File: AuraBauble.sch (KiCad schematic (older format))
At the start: 19 parts

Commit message: Switched Zener Diodes to a PRTR5V0U2X
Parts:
- removed D? (x5): 3.6V, symbol Device:D_Zener
- added D?: PRTR5V0U2X_215, digikey-footprints:TO-253-4, symbol dk_TVS-Diodes:PRTR5V0U2X_215
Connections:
- wire segments 78 -> 68
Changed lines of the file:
@@
 	9500 2100 9750 2100
 Connection ~ 9750 2100
-Wire Wire Line
-	9750 2100 10250 2100
-Wire Wire Line
-	9900 900  10250 900
 Connection ~ 9900 900
 Wire Wire Line
 	9900 900  9900 850
 Wire Wire Line
-	10250 1650 10250 900
-Connection ~ 10250 900
-Wire Wire Line
-	10250 1950 10250 2100
-Wire Wire Line
-	10250 2100 10550 2100
-Wire Wire Line
-	10550 1950 10550 2100
-Connection ~ 10550 2100
-Wire Wire Line
-	10550 2100 10850 2100
-Wire Wire Line
-	10850 1950 10850 2100
-Wire Wire Line
-	10850 1650 10850 1400
-Connection ~ 10850 1400
-Wire Wire Line
-	10850 1400 10850 1250
-$Comp
-L Device:D_Zener D?
-U 1 1 5F610AD1
-P 10850 1800
-F 0 "D?" V 10804 1880 50  0000 L CNN
-F 1 "3.6V" V 10895 1880 50  0000 L CNN
-F 2 "" H 10850 1800 50  0001 C CNN
-F 3 "~" H 10850 1800 50  0001 C CNN
-	1    10850 1800
-	0    1    1    0
-$EndComp
-$Comp
-L Device:D_Zener D?
-U 1 1 5F6110CF
-P 10550 1800
-F 0 "D?" V 10504 1880 50  0000 L CNN
-F 1 "3.6V" V 10595 1880 50  0000 L CNN
-F 2 "" H 10550 1800 50  0001 C CNN
-F 3 "~" H 10550 1800 50  0001 C CNN
-	1    10550 1800
-	0    1    1    0
-$EndComp
-$Comp
-L Device:D_Zener D?
-U 1 1 5F6115F3
-P 10250 1800
-F 0 "D?" V 10204 1880 50  0000 L CNN
-F 1 "3.6V" V 10295 1880 50  0000 L CNN
-F 2 "" H 10250 1800 50  0001 C CNN
-F 3 "~" H 10250 1800 50  0001 C CNN
-	1    10250 1800
-	0    1    1    0
-$EndComp
-Wire Wire Line
-	9500 1400 10850 1400
-Wire Wire Line
-	10250 900  10550 900
-Wire Wire Line
-	10850 1400 10950 1400
-Wire Wire Line
-	9500 1300 10550 1300
-Wire Wire Line
-	10550 1650 10550 1300
-Connection ~ 10550 1300
-Wire Wire Line
-	10550 1300 10950 1300
-Wire Wire Line
-	10550 1300 10550 1250
-Wire Wire Line
-	10550 950  10550 900
-Connection ~ 10550 900
-Wire Wire Line
-	10550 900  10850 900
-Wire Wire Line
-	10850 950  10850 900
-$Comp
-L Device:D_Zener D?
-U 1 1 5F626D93
-P 10850 1100
-F 0 "D?" V 10804 1180 50  0000 L CNN
-F 1 "3.6V" V 10895 1180 50  0000 L CNN
-F 2 "" H 10850 1100 50  0001 C CNN
-F 3 "~" H 10850 1100 50  0001 C CNN
-	1    10850 1100
-	0    1    1    0
-$EndComp
-$Comp
-L Device:D_Zener D?
-U 1 1 5F62603B
-P 10550 1100
-F 0 "D?" V 10504 1180 50  0000 L CNN
-F 1 "3.6V" V 10595 1180 50  0000 L CNN
-F 2 "" H 10550 1100 50  0001 C CNN
-F 3 "~" H 10550 1100 50  0001 C CNN
-	1    10550 1100
-	0    1    1    0
-$EndComp
+	10750 1950 10750 2100
 Wire Wire Line
 	10100 1800 10100 2200
@@
 	9200 1800 9500 1800
 Connection ~ 9500 1800
-Connection ~ 10250 2100
 Wire Notes Line
 	8750 1750 10000 1750
@@
 Text Notes 8850 4350 0    50   ~ 0
 Programmer may\nhave pullup.
+$Comp
+L dk_TVS-Diodes:PRTR5V0U2X_215 D?
+U 1 1 5F64F554
+P 10550 1450
+F 0 "D?" V 10800 1750 60  0000 L CNN
+F 1 "PRTR5V0U2X_215" H 10150 1950 60  0000 L CNN
+F 2 "digikey-footprints:TO-253-4" H 10750 1650 60  0001 L CNN
+F 3 "https://assets.nexperia.com/documents/data-sheet/PRTR5V0U2X.pdf" H 10750 1750 60  0001 L CNN
+F 4 "1727-3884-1-ND" H 10750 1850 60  0001 L CNN "Digi-Key_PN"
+F 5 "PRTR5V0U2X,215" H 10750 1950 60  0001 L CNN "MPN"
+F 6 "Circuit Protection" H 10750 2050 60  0001 L CNN "Category"
+F 7 "TVS - Diodes" H 10750 2150 60  0001 L CNN "Family"
+F 8 "https://assets.nexperia.com/documents/data-sheet/PRTR5V0U2X.pdf" H 10750 2250 60  0001 L CNN "DK_Datasheet_Link"
+F 9 "/product-detail/en/nexperia-usa-inc/PRTR5V0U2X,215/1727-3884-1-ND/1589981" H 10750 2350 60  0001 L CNN "DK_Detail_Page"
+F 10 "TVS DIODE 5.5V SOT143B" H 10750 2450 60  0001 L CNN "Description"
+F 11 "Nexperia USA Inc." H 10750 2550 60  0001 L CNN "Manufacturer"
+F 12 "Active" H 10750 2650 60  0001 L CNN "Status"
+	1    10550 1450
+	0    1    -1   0
+$EndComp
+Wire Wire Line
+	9500 1400 10250 1400
+Wire Wire Line
+	9500 1300 10250 1300
+Wire Wire Line
+	9900 900  10750 900
+Wire Wire Line
+	10750 900  10750 950
+Wire Wire Line
+	9750 2100 10750 2100
+Wire Wire Line
+	10250 1300 10250 950
+Wire Wire Line
+	10250 950  10350 950
+Wire Wire Line
+	10250 1400 10250 1950
+Wire Wire Line
+	10250 1950 10350 1950
 $EndSCHEMATC

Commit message: Power work.
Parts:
- added D1: BAT54XV2T1G, symbol Device:D_Schottky
- added Q1: Q_NMOS_DGS, symbol Device:Q_NMOS_DGS
- added R1: 1MΩ, symbol Device:R_US
- added R2: 330Ω, symbol Device:R_US
- added U1: LP5912-3.3DRV, Package_SON:WSON-6-1EP_2x2mm_P0.65mm_EP1x1.6mm_ThermalVias, symbol Regulator_Linear:LP5912-3.3DRV
- gave numbers to parts that had none: 15
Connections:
- net GND: now also D2.1 (GND), Q1.3 (S), R1.1, U1.5 (GND), U1.7 (EP)
- net VBUS: now also R2.2, U1.6 (IN)
- net VCC: now also D1.1 (K), U1.1 (OUT); no longer J2.5 (Vref)
- net MOSI: now reaches U2.A3 (PA04)
- net SCK: now reaches U2.A4 (PA06)
- net MISO: now reaches U2.B2 (PA05)
- net ~SS~: now reaches U2.B3 (PA07)
- net USB_POWER: now reaches U2.D3 (PA23)
- net USB_POWER: now also U1.3 (PG)
- net at C5.2, J1.5 (Shield), R4.1: no longer D2.1 (GND)
- new net: Q1.1 (D), R2.1, U1.4 (EN)
- new net +3V3: D1.2 (A), J2.5 (Vref), Q1.2 (G), R1.2
- no-connect marks 1 -> 11
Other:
- note added: "NYI"
- note added: "SPI For ARGB LEDs [26]"
- moved on the sheet: R3

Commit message: Schematic nearly r0.
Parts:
- removed Q1: Q_NMOS_DGS, symbol Device:Q_NMOS_DGS
- added BP1: Close If Option B Selected, symbol Jumper:SolderJumper_2_Open
- added C1, C2: 4.7µF, Capacitor_SMD:C_0603_1608Metric, symbol Device:C
- added D1, D3, D4, D5: SK6805, LED_SMD:LED_SK6812_EC15_1.5x1.5mm, symbol LED:WS2812B
- added J1: Bauble-Expando!, symbol Connector_Generic:Conn_01x04
- added TP1, TP2, TP3, TP4, TP5, TP6, TP7, TP8: TestPoint_Small, TestPoint:TestPoint_Pad_D1.0mm, symbol Connector:TestPoint_Small
- added U1: 74LVC1G02SE-7, Package_TO_SOT_SMD:SOT-353_SC-70-5, symbol AuraBauble_Custom:74LVC1G02
- C3: renamed from C1; value *DNP* -> 7.5pF; footprint (none) -> Capacitor_SMD:C_0603_1608Metric
- C4: renamed from C2; value *DNP* -> 7.5pF; footprint (none) -> Capacitor_SMD:C_0603_1608Metric
- C5: renamed from C3; footprint (none) -> Capacitor_SMD:C_0603_1608Metric
- C6: renamed from C4; footprint (none) -> Capacitor_SMD:C_0603_1608Metric
- C7: renamed from C5; footprint (none) -> Capacitor_SMD:C_0603_1608Metric
- C8: renamed from C6; footprint (none) -> Capacitor_SMD:C_0603_1608Metric
- D2: renamed from D1; footprint (none) -> Diode_SMD:D_SOD-523; Digi-Key (none) -> BAT54XV2T1GOSCT-ND
- J3: renamed from J2; footprint (none) -> Connector_DebugEdge:DebugEdge_2x05_Target
- R1: value 1MΩ -> 100MΩ; footprint (none) -> Resistor_SMD:R_0603_1608Metric
- R2: value 330Ω -> 100kΩ; footprint (none) -> Resistor_SMD:R_0603_1608Metric
- R3, R4, R5: footprint (none) -> Resistor_SMD:R_0603_1608Metric
- SW1: value RESET_SW -> KXT 321 LHS; footprint (none) -> Button_Switch_SMD:SW_SPST_CK_KXT3; Digi-Key (none) -> CKN10778CT-ND
- U2: renamed from U1; Digi-Key (none) -> 296-44153-1-ND
- Y1: value *DNP* -> FC-135R; footprint (none) -> Crystal:Crystal_SMD_3215-2Pin_3.2x1.5mm; Digi-Key (none) -> FC-135 32.7680KA-AG5
- renumbered D2 to D6, J1 to J2, U2 to U3
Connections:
- net +3V3: now also U1.1
- net GND: now also C1.2, C2.1, D1.3 (VSS), D3.3 (VSS), D4.3 (VSS), D5.3 (VSS), J1.4 (Pin_4), U1.2, U1.3 (GND)
- net MISO: now also TP1.1
- net MOSI: now also BP1.1 (A), D1.4 (DIN)
- net SCK: now also J1.3 (Pin_3)
- net USB_POWER: now also R2.2
- net VBUS: now also C1.1, U1.6 (VCC); no longer R2.2
- net VCC: now also R2.1, C2.2, D1.1 (VDD), D3.1 (VDD), D4.1 (VDD), D5.1 (VDD), J1.1 (Pin_1)
- net ~SS~: now also TP2.1
- net at U3.A1 (PA02): now also TP3.1
- net at U3.A2 (PA03): now also TP4.1
- net at U3.C3 (PA16): now also TP7.1
- net at U3.D4 (PA14): now also TP5.1
- net at U3.E3 (PA22): now also TP8.1
- net at U3.E4 (PA15): now also TP6.1
- net at U2.4 (EN): now also U1.4; no longer R2.1
- new net: D1.2 (DOUT), D3.4 (DIN)
- new net: D3.2 (DOUT), D4.4 (DIN)
- new net: D4.2 (DOUT), D5.4 (DIN)
- new net: BP1.2 (B), D5.2 (DOUT), J1.2 (Pin_2)
- no-connect marks 11 -> 1
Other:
- note added: "Debug Power Mux"
- note added: "Ext XTAL [37.6.(2|3)]\nClose to uC as able."
- note added: "Option A: On-board Lights"
- note added: "Option B: On-board Bypass"
- note added: "PINMUX:C"
- note added: "PINMUX:G"
- note added: "Prefer X7R Decoupling Caps"
- note added: "SPI For ARGB LEDs [26]\nPINMUX:C"
- note added: "Single Wire Debug (SWD) [37.7]\nPINMUX: G"
- note added: "Unused SPI Signals"
- note added: "VBUS LDO"
- note removed: "Ext XTAL [37.6.(2|3)]"
- note removed: "NYI"
- note removed: "SPI For ARGB LEDs [26]"
- note removed: "Single Wire Debug (SWD) [37.7]"
- moved on the sheet: C3, C4, C5, C6, C8, D2, J3, R1, R3, R5, SW1, U2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

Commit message: Moved to the QFN SAMD.
Looks like oshpark can't do the tolerances for the WLCSP.

Gave it my all trying to route it as a 2-layer, but doesn't look like I can do it and stay as tiny as I want. Tomorrow we'll go 4 layer.
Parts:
- removed TP5, TP6, TP7, TP8: TestPoint_Small, TestPoint:TestPoint_Pad_D1.0mm, symbol Connector:TestPoint_Small
- removed U3: ATSAMD11D14A-U, Package_CSP:WLCSP-20_1.934x2.434mm_Layout4x5_P0.4mm, symbol MCU_Microchip_SAMD:ATSAMD11D14A-U
- added CT1, CT2, CT3: CT_Capacitive_Touch_Point_2, Jumper:SolderJumper-2_P1.3mm_Open_RoundedPad1.0x1.5mm, symbol AuraBauble_Custom:CT_Capacitive_Touch_Point_2
- added NT1: Net-Tie_2, NetTie:NetTie-2_THT_Pad1.0mm, symbol Device:Net-Tie_2
- added U1: ATSAMD11D14A-M, Package_DFN_QFN:QFN-24-1EP_4x4mm_P0.5mm_EP2.6x2.6mm, symbol MCU_Microchip_SAMD:ATSAMD11D14A-M
- BP1: footprint (none) -> Jumper:SolderJumper-2_P1.3mm_Open_TrianglePad1.0x1.5mm
- C1, C2, C5, C6, C7, C8: footprint Capacitor_SMD:C_0603_1608Metric -> Capacitor_SMD:C_0402_1005Metric
- C3, C4: value 7.5pF -> 8.2pF; footprint Capacitor_SMD:C_0603_1608Metric -> Capacitor_SMD:C_0402_1005Metric
- J1: footprint (none) -> AuraBauble:BaubleExpando
- J2: footprint (none) -> AuraBauble:USB_A_Plug_Edge
- R1, R2, R3, R4, R5: footprint Resistor_SMD:R_0603_1608Metric -> Resistor_SMD:R_0402_1005Metric
- U3: renamed from U1; footprint Package_TO_SOT_SMD:SOT-353_SC-70-5 -> Package_TO_SOT_SMD:SOT-363_SC-70-6
- renumbered D2 to D1, D1 to D2
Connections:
- net GND: now also U1.24 (VDD)
- net MISO: now also U1.16 (PA23)
- net MOSI: now also U1.21 (PA24)
- net SCK: now also U1.15 (PA22)
- net USB_POWER: now also U1.4 (PA05)
- net VBUS: now also NT1.1
- net VCC: now also U1.23 (GND); no longer D2.1 (VDD), D3.1 (VDD), D4.1 (VDD), D5.1 (VDD), J1.1 (Pin_1)
- net ~SS~: now also U1.14 (PA17)
- net at TP3.1: now also U1.17 (PA27)
- net at TP4.1: now also U1.22 (PA25)
- net at C4.1, Y1.1: now also U1.8 (PA09/XOUT)
- net USB_DM renamed USB_D-
- net USB_D-: now also U1.3 (PA04)
- net USB_DP renamed USB_D+
- net USB_D+: now also U1.2 (PA03)
- new net TOUCHX: CT1.2 (B), CT2.2 (B), CT3.2 (B), U1.11 (PA14)
- new net TOUCH_Y_0: CT1.1 (A), U1.10 (PA11)
- new net TOUCH_Y_1: CT2.1 (A), U1.9 (PA10)
- new net TOUCH_Y_2: CT3.1 (A), U1.6 (PA07)
- new net VLED: D2.1 (VDD), D3.1 (VDD), D4.1 (VDD), D5.1 (VDD), J1.1 (Pin_1), NT1.2
- no-connect marks 1 -> 5
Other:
- note added: "32.768 kHz\n7pF\n±20PPM"
- note added: "Capacitive Touch\nPINMUX:B (PTC)"
- note added: "PINMUX:B\nPTC"
- note added: "VLED is VBUS"
- moved on the sheet: BP1, C3, C4, C5, C6, D2, D3, D4, D5, J1, TP1, TP2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

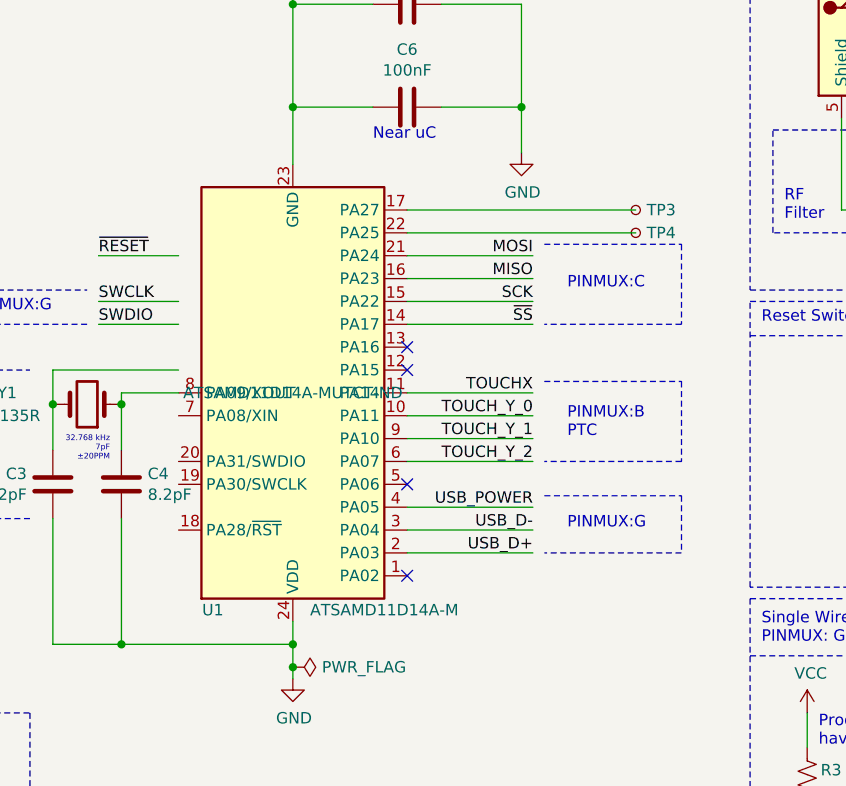
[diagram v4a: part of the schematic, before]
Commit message: Removed some test points.
Also flipped the uC, because somehow it flipped?
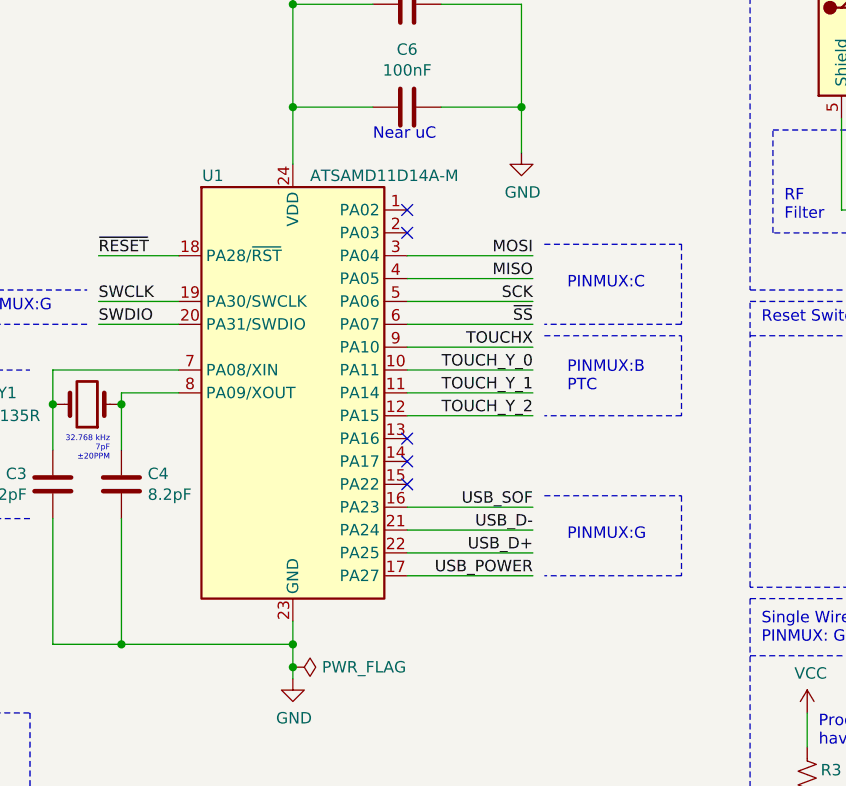
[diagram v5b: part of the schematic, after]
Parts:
- removed TP3, TP4: TestPoint_Small, TestPoint:TestPoint_Pad_D1.0mm, symbol Connector:TestPoint_Small
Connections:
- net GND: now also U1.23 (GND); no longer U1.24 (VDD)
- net MISO: now also U1.4 (PA05); no longer U1.16 (PA23)
- net MOSI: now also U1.3 (PA04); no longer U1.21 (PA24)
- net SCK: now also U1.5 (PA06); no longer U1.15 (PA22)
- net SWCLK: now also U1.19 (PA30/SWCLK)
- net SWDIO: now also U1.20 (PA31/SWDIO)
- net TOUCHX: now also U1.9 (PA10); no longer U1.11 (PA14)
- net TOUCH_Y_1: now also U1.11 (PA14); no longer U1.9 (PA10)
- net TOUCH_Y_2: now also U1.12 (PA15); no longer U1.6 (PA07)
- net USB_D+: now also U1.22 (PA25); no longer U1.2 (PA03)
- net USB_D-: now also U1.21 (PA24); no longer U1.3 (PA04)
- net USB_POWER: now also U1.17 (PA27); no longer U1.4 (PA05)
- net VCC: now also U1.24 (VDD); no longer U1.23 (GND)
- net ~RESET~: now also U1.18 (PA28/~RST)
- net ~SS~: now also U1.6 (PA07); no longer U1.14 (PA17)
- net at C3.1, Y1.2: now also U1.7 (PA08/XIN)
- new net USB_SOF: U1.16 (PA23)
- no-connect marks 5 -> 6
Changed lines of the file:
@@
 $EndComp
-Wire Wire Line
-	6700 1000 6700 1200
 Wire Wire Line
 	6700 1650 6700 1900
@@
 	1    0    0    -1
 $EndComp
-Wire Wire Line
-	6200 2500 5850 2500
 Wire Wire Line
 	6200 2600 5850 2600
@@
 Text Label 3650 2350 2    50   ~ 0
 USB_POWER
-Text Label 7750 3400 2    50   ~ 0
+Text Label 7750 3700 2    50   ~ 0
 USB_POWER
 Connection ~ 9650 1100
@@
 Text Notes 7900 2450 0    50   ~ 0
 PINMUX:C
-Text Notes 7900 3500 0    50   ~ 0
+Text Notes 7900 3550 0    50   ~ 0
 PINMUX:G
 Wire Notes Line
@@
 	7800 3350 8400 3350
 Wire Notes Line
-	8400 3350 8400 3600
-$Comp
-L Connector:TestPoint_Small TP3
-U 1 1 5FD10D71
-P 8200 2100
-F 0 "TP3" H 8248 2100 50  0000 L CNN
-F 1 "TestPoint_Small" H 8248 2055 50  0001 L CNN
-F 2 "TestPoint:TestPoint_Pad_D1.0mm" H 8400 2100 50  0001 C CNN
-F 3 "~" H 8400 2100 50  0001 C CNN
-	1    8200 2100
-	1    0    0    -1
-$EndComp
-$Comp
-L Connector:TestPoint_Small TP4
-U 1 1 5FD178B4
-P 8200 2200
-F 0 "TP4" H 8248 2200 50  0000 L CNN
-F 1 "TestPoint_Small" H 8248 2155 50  0001 L CNN
-F 2 "TestPoint:TestPoint_Pad_D1.0mm" H 8400 2200 50  0001 C CNN
-F 3 "~" H 8400 2200 50  0001 C CNN
-	1    8200 2200
-	1    0    0    -1
-$EndComp
-Wire Notes Line
-	8400 3600 7800 3600
-Wire Wire Line
-	7200 2100 8200 2100
-Wire Wire Line
-	7200 2200 8200 2200
+	8400 3350 8400 3700
+Wire Notes Line
+	8400 3700 7800 3700
 Text Notes 4700 3200 0    50   ~ 0
 Ext XTAL [37.6.(2|3)]\nClose to uC as able.
@@
 Wire Notes Line
 	5800 2600 5200 2600
-Wire Wire Line
-	6200 2800 5650 2800
 Wire Wire Line
 	5650 2800 5650 2950
@@
 Text Notes 5900 3200 2    25   ~ 0
 32.768 kHz\n7pF\n±20PPM
+Text Label 7750 2700 2    50   ~ 0
+TOUCHX
+Text Label 7750 2800 2    50   ~ 0
+TOUCH_Y_0
 Text Label 7750 2900 2    50   ~ 0
-TOUCHX
+TOUCH_Y_1
 Text Label 7750 3000 2    50   ~ 0
-TOUCH_Y_0
-Text Label 7750 3100 2    50   ~ 0
-TOUCH_Y_1
-Text Label 7750 3200 2    50   ~ 0
 TOUCH_Y_2
-Text Notes 7900 3100 0    50   ~ 0
+Text Notes 7900 2900 0    50   ~ 0
 PINMUX:B\nPTC
 Wire Notes Line
-	7800 2850 8400 2850
-Wire Notes Line
-	8400 2850 8400 3200
-Wire Notes Line
-	8400 3200 7800 3200
+	7800 2650 8400 2650
+Wire Notes Line
+	8400 2650 8400 3000
+Wire Notes Line
+	8400 3000 7800 3000
 Wire Wire Line
 	750  3950 1350 3950
@@
 Wire Wire Line
 	6700 3900 6700 4000
-$Comp
-L MCU_Microchip_SAMD:ATSAMD11D14A-M U1
-U 1 1 5FA830AE
-P 6700 2900
-F 0 "U1" H 6350 3850 50  0000 C CNN
-F 1 "ATSAMD11D14A-M" H 7100 3850 50  0000 C CNN
-F 2 "Package_DFN_QFN:QFN-24-1EP_4x4mm_P0.5mm_EP2.6x2.6mm" H 6700 1550 50  0001 C CNN
-F 3 "http://ww1.microchip.com/downloads/en/DeviceDoc/Atmel-42363-SAM-D11_Datasheet.pdf" H 6700 1900 50  0001 C CNN
-F 4 "ATSAMD11D14A-MUTCT-ND" H 6700 2900 50  0000 C CNN "Digi-Key"
-	1    6700 2900
-	1    0    0    1
-$EndComp
 Connection ~ 6700 4100
 Wire Wire Line
@@
 	7200 3500 7750 3500
 Wire Wire Line
-	7200 3400 7750 3400
-Wire Wire Line
-	7200 3200 7750 3200
-Wire Wire Line
-	7200 3100 7750 3100
+	7200 3700 7750 3700
 Wire Wire Line
 	7200 3000 7750 3000
 Wire Wire Line
 	7200 2900 7750 2900
+Wire Wire Line
+	7200 2800 7750 2800
+Wire Wire Line
+	7200 2700 7750 2700
 Wire Wire Line
 	5950 4000 6700 4000
@@
 Wire Wire Line
 	6700 4000 6700 4100
-NoConn ~ 7200 2700
-NoConn ~ 7200 2800
-NoConn ~ 7200 3700
+NoConn ~ 7200 3100
+NoConn ~ 7200 3200
 NoConn ~ 7200 3300
+Wire Wire Line
+	6200 2800 5650 2800
+Wire Wire Line
+	6200 2500 5850 2500
+$Comp
+L MCU_Microchip_SAMD:ATSAMD11D14A-M U1
+U 1 1 5FA830AE
+P 6700 2900
+F 0 "U1" H 6350 3850 50  0000 C CNN
+F 1 "ATSAMD11D14A-M" H 7100 3850 50  0000 C CNN
+F 2 "Package_DFN_QFN:QFN-24-1EP_4x4mm_P0.5mm_EP2.6x2.6mm" H 6700 1550 50  0001 C CNN
+F 3 "http://ww1.microchip.com/downloads/en/DeviceDoc/Atmel-42363-SAM-D11_Datasheet.pdf" H 6700 1900 50  0001 C CNN
+F 4 "ATSAMD11D14A-MUTCT-ND" H 6650 2800 50  0001 C CNN "Digi-Key"
+	1    6700 2900
+	1    0    0    -1
+$EndComp
+Wire Wire Line
+	6700 1000 6700 1200
+Text Label 7750 3400 2    50   ~ 0
+USB_SOF
+Wire Wire Line
+	7200 3400 7750 3400
+NoConn ~ 7200 2100
+NoConn ~ 7200 2200
 $EndSCHEMATC

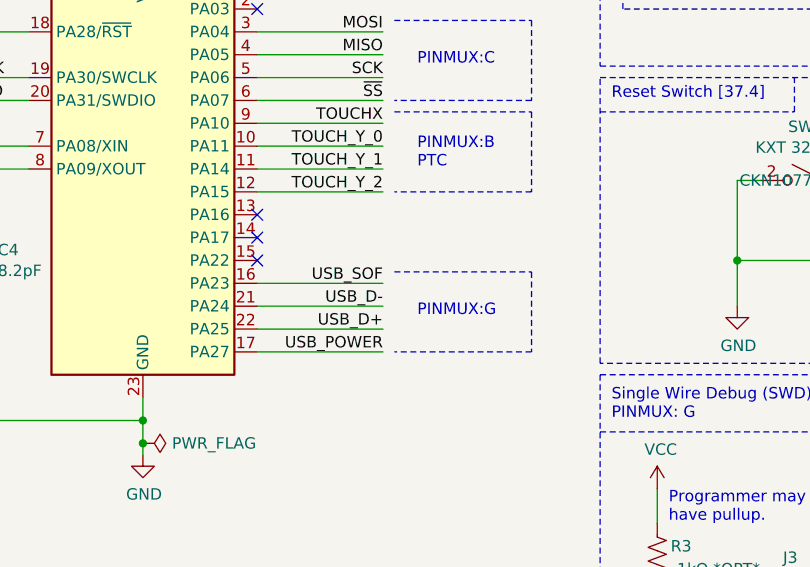
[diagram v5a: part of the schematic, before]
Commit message: Added TP for USB SOF.
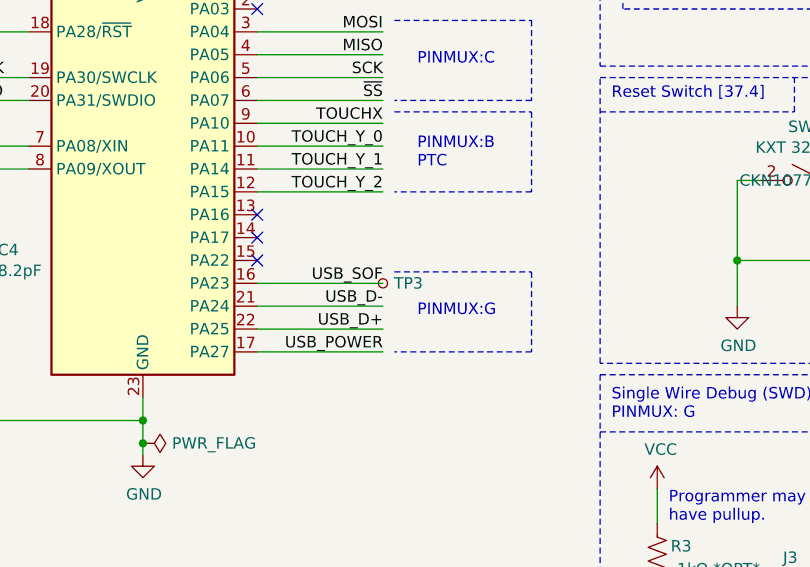
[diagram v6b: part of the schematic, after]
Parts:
- added TP3: TestPoint_Small, TestPoint:TestPoint_Pad_D1.0mm, symbol Connector:TestPoint_Small
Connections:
- net USB_SOF: now also TP3.1
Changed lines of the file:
@@
 NoConn ~ 7200 2100
 NoConn ~ 7200 2200
+$Comp
+L Connector:TestPoint_Small TP3
+U 1 1 5F6C4664
+P 7750 3400
+F 0 "TP3" H 7798 3400 50  0000 L CNN
+F 1 "TestPoint_Small" H 7798 3355 50  0001 L CNN
+F 2 "TestPoint:TestPoint_Pad_D1.0mm" H 7950 3400 50  0001 C CNN
+F 3 "~" H 7950 3400 50  0001 C CNN
+	1    7750 3400
+	1    0    0    -1
+$EndComp
 $EndSCHEMATC
